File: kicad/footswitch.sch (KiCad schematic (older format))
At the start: 72 parts, among them IC1 ATMEGA328P-A, P1 Atmega right, P2 Atmega top, P3 Programming header, P4 Atmega bottom, P5 Atmega left, P6 Pot hdr, P7 App select, Q1 BSS214NWH6327XTSA1, Q2 BSS214NWH6327XTSA1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

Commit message: Remove OR gates; add version and authors to silk screen
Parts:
- removed C15, C16: 10uF, Capacitors_SMD:C_1206_HandSoldering, symbol C_Small
- removed P7: App select, Pin_Headers:Pin_Header_Straight_1x02_Pitch2.54mm, symbol CONN_01X02
- removed U2, U3: CD4072BM96, Housings_SOIC:SOIC-14_3.9x8.7mm_Pitch1.27mm, symbol CD4072BM96
- SW4: footprint switches:100SP4T1B1M1QEH -> Pin_Headers:Pin_Header_Straight_1x03_Pitch2.54mm
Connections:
- net A1: now also R21.2, SW7.2 (B); no longer R19.2, SW8.2 (B)
- net A2: now also R23.2, SW6.2 (B); no longer R21.2, SW7.2 (B)
- net A3: now also R24.2, SW5.2 (B); no longer R23.2, SW6.2 (B)
- net A6: no longer R20.2, R8.2, SW4.3 (C)
- net D2: now also R4.1, U1.3 (CE)
- net D3: now also R5.1, U1.4 (CSN); no longer R9.2, SW4.1 (A)
- net D6: now also R20.2, R8.2, SW4.3 (C); no longer R4.1, U1.3 (CE)
- net D7: now also R22.2, R9.2, SW4.1 (A); no longer R5.1, U1.4 (CSN)
- net D8: now also R19.2, SW8.2 (B); no longer R22.2, R7.2, SW3.2 (B)
- net SCL: now also R7.2, SW3.2 (B); no longer R6.2, SW2.2 (B)
- net SDA: now also R6.2, SW2.2 (B); no longer R24.2, SW5.2 (B)
- no-connect marks 10 -> 5
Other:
- moved on the sheet: AFF1, BT1, C12, C14, P1, P2, P3, P4, P5, P6, Q1, Q2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

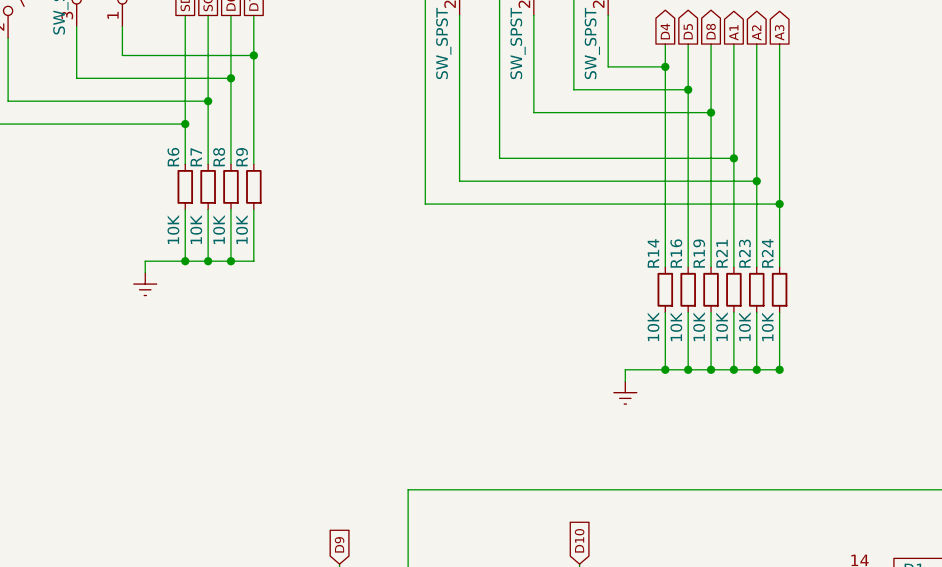
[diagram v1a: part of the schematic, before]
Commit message: Change resistor values to 1M to conserve power
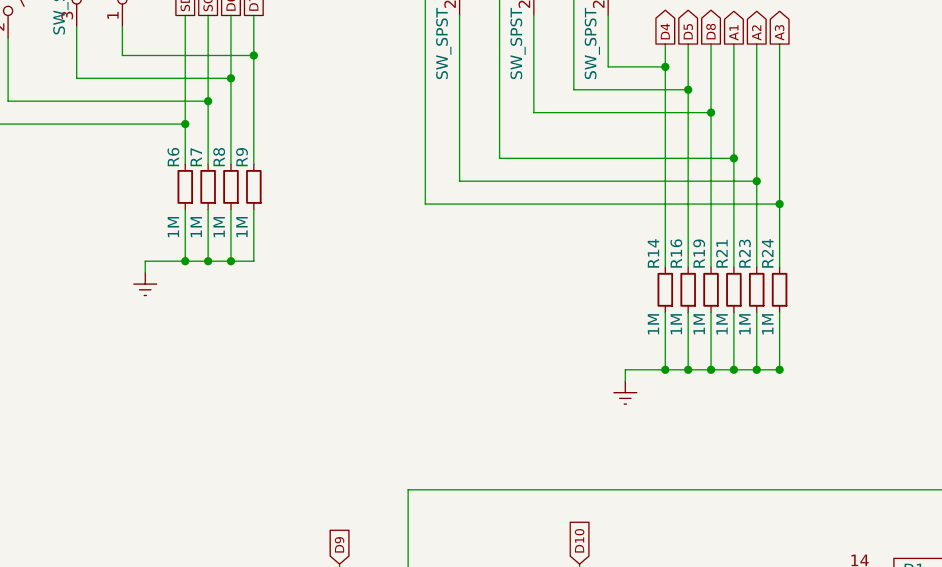
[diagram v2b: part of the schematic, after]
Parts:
- R14, R16, R19, R21, R23, R24, R6, R7, R8, R9: value 10K -> 1M
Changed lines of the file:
@@
 P 8050 3100
 F 0 "R14" V 8100 2875 50  0000 L CNN
-F 1 "10K" V 8100 3200 50  0000 L CNN
+F 1 "1M" V 8100 3200 50  0000 L CNN
 F 2 "Resistors_SMD:R_1206_HandSoldering" H 8050 3100 50  0001 C CNN
 F 3 "" H 8050 3100 50  0000 C CNN
@@
 P 8150 3100
 F 0 "R16" V 8200 2875 50  0000 L CNN
-F 1 "10K" V 8200 3200 50  0000 L CNN
+F 1 "1M" V 8200 3200 50  0000 L CNN
 F 2 "Resistors_SMD:R_1206_HandSoldering" H 8150 3100 50  0001 C CNN
 F 3 "" H 8150 3100 50  0000 C CNN
@@
 P 8250 3100
 F 0 "R19" V 8300 2875 50  0000 L CNN
-F 1 "10K" V 8300 3200 50  0000 L CNN
+F 1 "1M" V 8300 3200 50  0000 L CNN
 F 2 "Resistors_SMD:R_1206_HandSoldering" H 8250 3100 50  0001 C CNN
 F 3 "" H 8250 3100 50  0000 C CNN
@@
 P 8350 3100
 F 0 "R21" V 8400 2875 50  0000 L CNN
-F 1 "10K" V 8400 3200 50  0000 L CNN
+F 1 "1M" V 8400 3200 50  0000 L CNN
 F 2 "Resistors_SMD:R_1206_HandSoldering" H 8350 3100 50  0001 C CNN
 F 3 "" H 8350 3100 50  0000 C CNN
@@
 P 8450 3100
 F 0 "R23" V 8500 2875 50  0000 L CNN
-F 1 "10K" V 8500 3200 50  0000 L CNN
+F 1 "1M" V 8500 3200 50  0000 L CNN
 F 2 "Resistors_SMD:R_1206_HandSoldering" H 8450 3100 50  0001 C CNN
 F 3 "" H 8450 3100 50  0000 C CNN
@@
 P 8550 3100
 F 0 "R24" V 8600 2875 50  0000 L CNN
-F 1 "10K" V 8600 3200 50  0000 L CNN
+F 1 "1M" V 8600 3200 50  0000 L CNN
 F 2 "Resistors_SMD:R_1206_HandSoldering" H 8550 3100 50  0001 C CNN
 F 3 "" H 8550 3100 50  0000 C CNN
@@
 P 6050 2650
 F 0 "R7" V 6100 2475 50  0000 L CNN
-F 1 "10K" V 6100 2775 50  0000 L CNN
+F 1 "1M" V 6100 2775 50  0000 L CNN
 F 2 "Resistors_SMD:R_1206_HandSoldering" H 6050 2650 50  0001 C CNN
 F 3 "" H 6050 2650 50  0000 C CNN
@@
 P 6150 2650
 F 0 "R8" V 6200 2475 50  0000 L CNN
-F 1 "10K" V 6200 2775 50  0000 L CNN
+F 1 "1M" V 6200 2775 50  0000 L CNN
 F 2 "Resistors_SMD:R_1206_HandSoldering" H 6150 2650 50  0001 C CNN
 F 3 "" H 6150 2650 50  0000 C CNN
@@
 P 6250 2650
 F 0 "R9" V 6300 2475 50  0000 L CNN
-F 1 "10K" V 6300 2775 50  0000 L CNN
+F 1 "1M" V 6300 2775 50  0000 L CNN
 F 2 "Resistors_SMD:R_1206_HandSoldering" H 6250 2650 50  0001 C CNN
 F 3 "" H 6250 2650 50  0000 C CNN
@@
 P 5950 2650
 F 0 "R6" V 6000 2475 50  0000 L CNN
-F 1 "10K" V 6000 2775 50  0000 L CNN
+F 1 "1M" V 6000 2775 50  0000 L CNN
 F 2 "Resistors_SMD:R_1206_HandSoldering" H 5950 2650 50  0001 C CNN
 F 3 "" H 5950 2650 50  0000 C CNN
